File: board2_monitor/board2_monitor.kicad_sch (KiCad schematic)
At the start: 83 parts, among them J1 Conn_02x04_Odd_Even, J2 Conn_02x04_Odd_Even, J3 Conn_01x04, J4 Screw_Terminal_01x08, SW1 WAKE, U1 IS31FL3731-SA

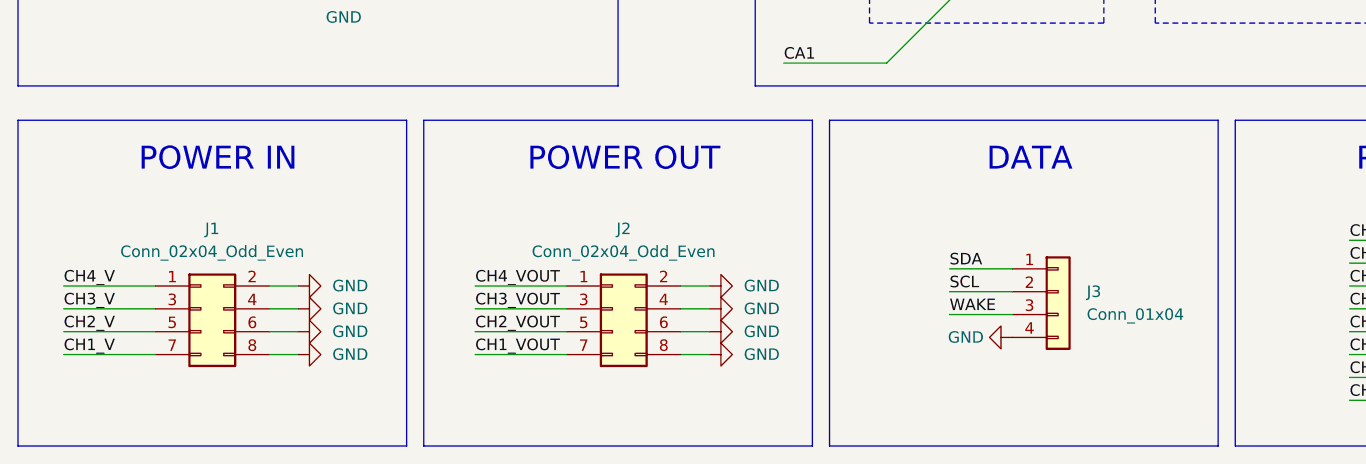
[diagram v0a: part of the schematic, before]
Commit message: connector fixes to the boards - swapped headers with sockets and vice versa. had to adjust the schematics too but no big changes, everything still connected appropriately
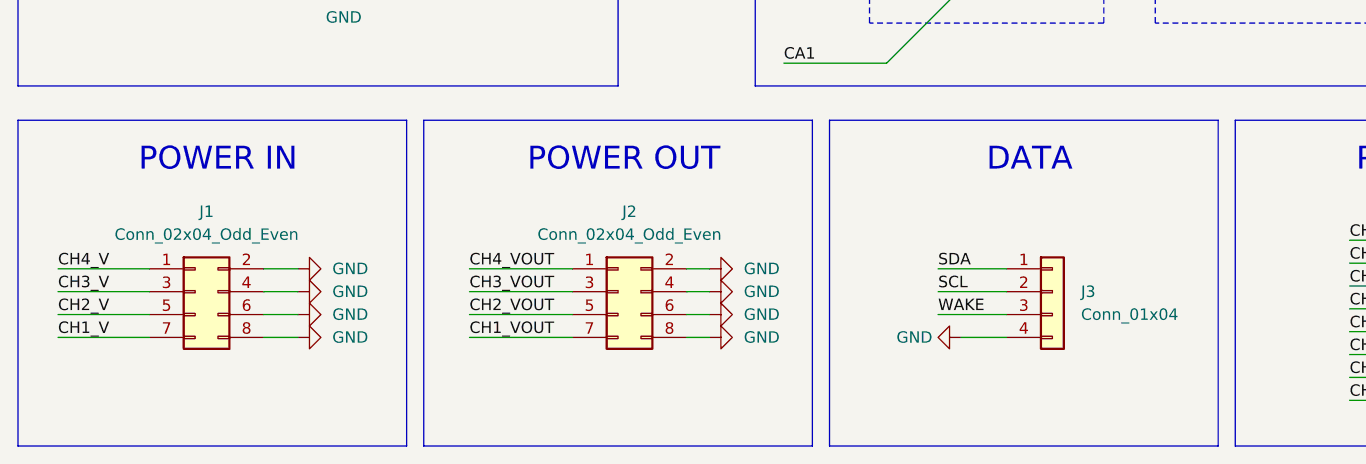
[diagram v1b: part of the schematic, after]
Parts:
- J1, J2: footprint Connector_PinSocket_2.54mm:PinSocket_2x04_P2.54mm_Vertical -> Connector_PinHeader_2.54mm:PinHeader_2x04_P2.54mm_Vertical
- J3: footprint Connector_PinSocket_2.54mm:PinSocket_1x04_P2.54mm_Vertical -> Connector_PinHeader_2.54mm:PinHeader_1x04_P2.54mm_Vertical
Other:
- moved on the sheet: J1, J2, J3
